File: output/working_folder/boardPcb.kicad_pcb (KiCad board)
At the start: 2 copper layers, 188.6 x 119.9 mm, 118 parts

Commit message: finished initial layout; pending 3 reviews
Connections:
- S25 pad 1: P14 -> P16
- S26 pad 1: P14 -> P16
- S27 pad 1: P16 -> P14
- S28 pad 1: P14 -> P16
- S29 pad 1: P16 -> P14
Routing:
- net VCC: track 10.3 -> 977.4 mm, vias 0 -> 32
- net P15: track 0.00 -> 879.4 mm, vias 0 -> 56
- net GND: track 30.9 -> 901.8 mm, vias 0 -> 66
- net P8: track 0.00 -> 800.1 mm, vias 0 -> 37
- net P20: track 34.6 -> 382.8 mm, vias 0 -> 2
- net P19: track 34.6 -> 346.8 mm, vias 0 -> 2
- net P21: track 30.2 -> 292.5 mm
- net P2: track 39.5 -> 246.9 mm
- net P18: track 25.9 -> 219.2 mm
- net P3: track 39.5 -> 227.8 mm
- net P4: track 39.6 -> 203.4 mm
- net P5: track 39.5 -> 179.0 mm
- net P6: track 39.5 -> 154.8 mm
- net P16: track 19.8 -> 119.9 mm
- net P7: track 39.5 -> 136.7 mm
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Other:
- board text added: "P21"

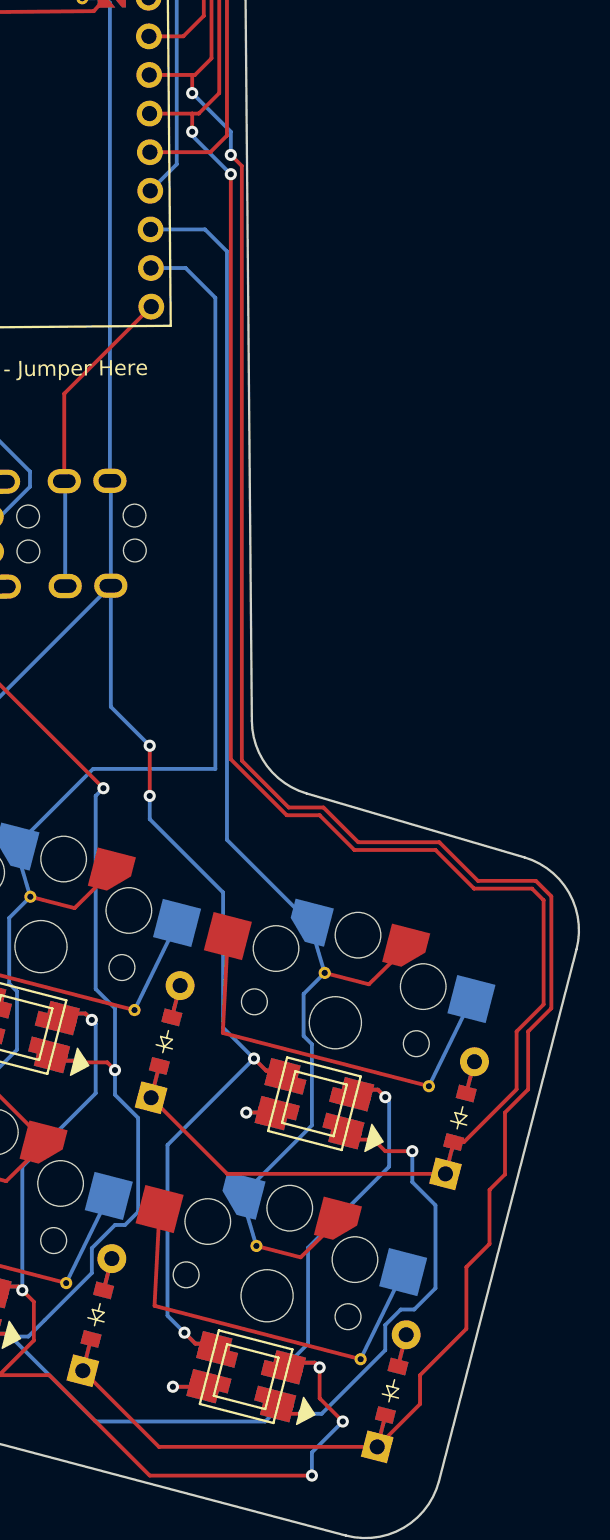
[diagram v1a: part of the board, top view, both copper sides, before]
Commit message: tweak two remove 2 redundant vias
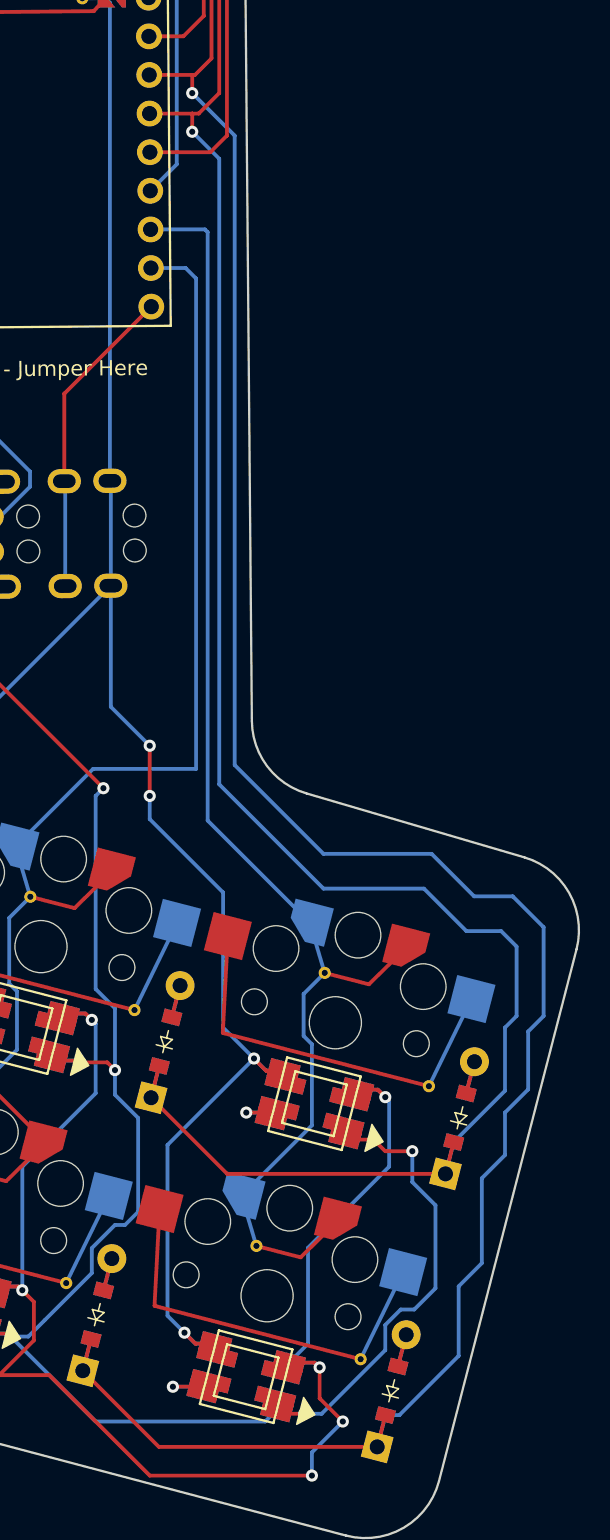
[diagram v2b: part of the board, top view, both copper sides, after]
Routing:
- net P20: track 382.8 -> 379.6 mm, vias 2 -> 1
- net P19: track 346.8 -> 343.7 mm, vias 2 -> 1
- net P16: track 119.9 -> 118.1 mm
